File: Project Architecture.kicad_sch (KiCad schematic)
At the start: 0 parts

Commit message: power supply first draft
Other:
- sheet Power supply ports: added +20 V; removed none
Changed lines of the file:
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@@
+			)
+		)
+		(pin "+20 V" passive
+			(at 237.49 57.15 0)
+			(effects
+				(font
+					(size 1.27 1.27)
+				)
+				(justify right)
 			)
 		)

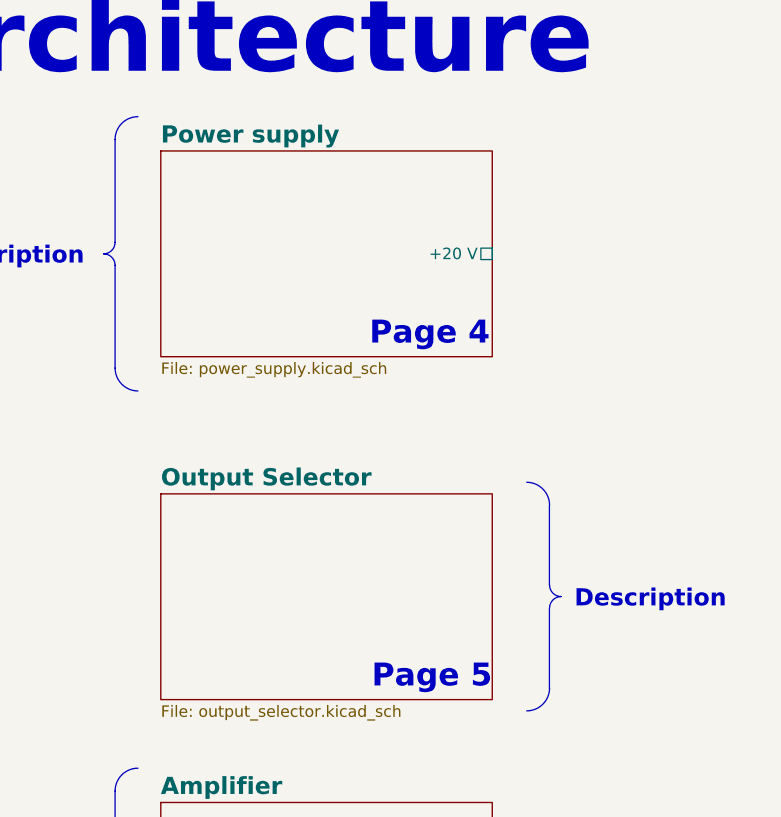
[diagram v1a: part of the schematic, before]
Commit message: Add output selector
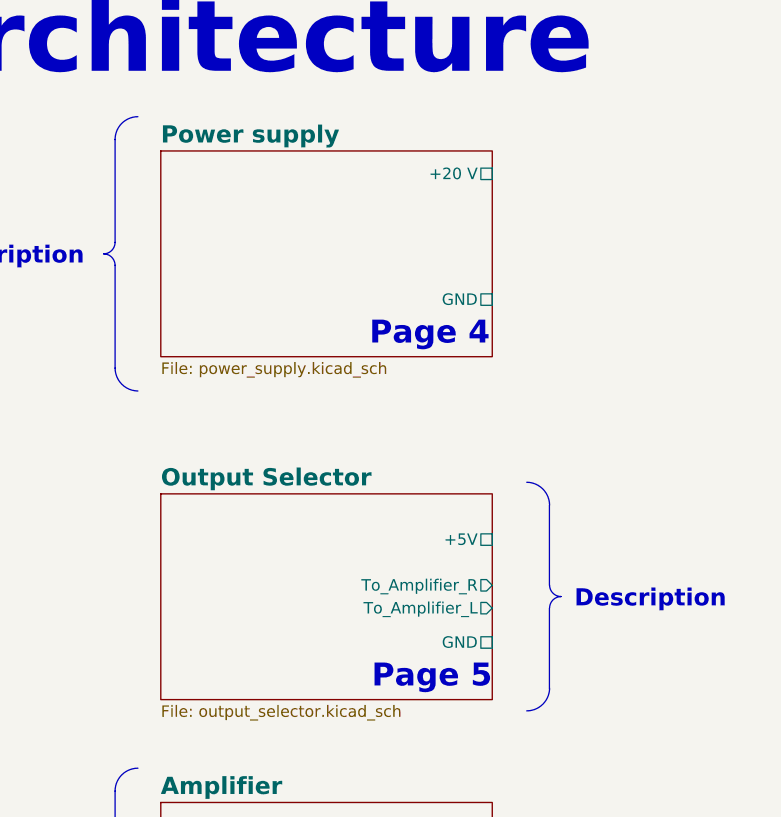
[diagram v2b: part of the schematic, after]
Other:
- sheet Output Selector ports: added +5V, GND, To_Amplifier_L, To_Amplifier_R; removed none
- sheet Power supply ports: added GND; removed none
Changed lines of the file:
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@@
+			)
+		)
+		(pin "To_Amplifier_R" output
+			(at 237.49 93.98 0)
+			(effects
+				(font
+					(size 1.27 1.27)
+				)
+				(justify right)
+			)
+		)
+		(pin "To_Amplifier_L" output
+			(at 237.49 96.52 0)
+			(effects
+				(font
+					(size 1.27 1.27)
+				)
+				(justify right)
+			)
+		)
+		(pin "+5V" passive
+			(at 237.49 88.9 0)
+			(effects
+				(font
+					(size 1.27 1.27)
+				)
+				(justify right)
+			)
+		)
+		(pin "GND" passive
+			(at 237.49 100.33 0)
+			(effects
+				(font
+					(size 1.27 1.27)
+				)
+				(justify right)
 			)
 		)
@@
 		)
 		(pin "+20 V" passive
-			(at 237.49 57.15 0)
+			(at 237.49 48.26 0)
 			(effects
 				(font
+					(size 1.27 1.27)
+				)
+				(justify right)
+			)
+		)
+		(pin "GND" passive
+			(at 237.49 62.23 0)
+			(effects
+				(font

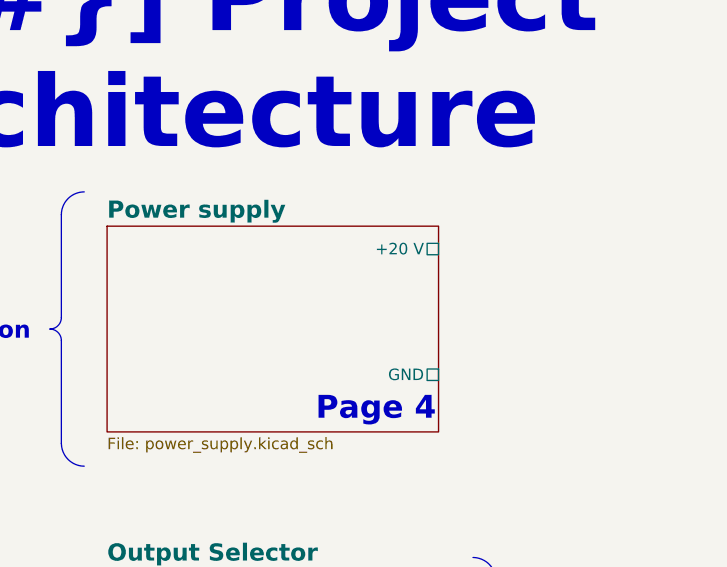
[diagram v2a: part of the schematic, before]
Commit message: add 5V regulator
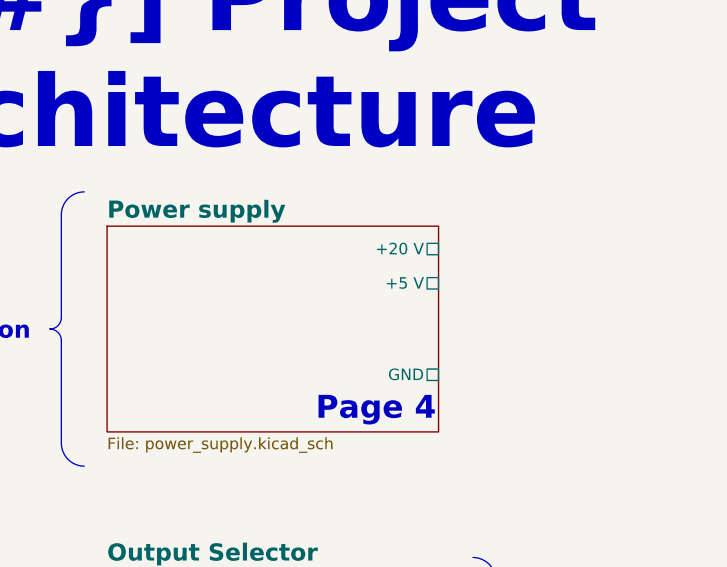
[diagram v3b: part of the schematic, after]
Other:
- sheet Power supply ports: added +5 V; removed none
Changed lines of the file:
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@@
+			)
+		)
+		(pin "+5 V" passive
+			(at 237.49 52.07 0)
+			(effects
+				(font
+					(size 1.27 1.27)
+				)
+				(justify right)
 			)
 		)

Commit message: complete wiring
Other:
- sheet Amplifier ports: added +20 V, From_Selector_L, From_Selector_R, GND, ~{AmpSD}; removed none
- sheet Output Selector ports: added ~{AmpSD}; removed none

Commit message: finish pcb and generate production file
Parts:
- added H1, H2, H3, H4: MountingHole_Pad, MountingHole:MountingHole_3.2mm_M3_Pad_Via, symbol Mechanical:MountingHole_Pad
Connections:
- net Amplifier/GND: now also H1.1, H2.1, H3.1, H4.1
